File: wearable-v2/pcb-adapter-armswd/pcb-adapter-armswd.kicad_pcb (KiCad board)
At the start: 2 copper layers, 10.6 x 20.8 mm, 2 parts, among them J1 Arm SWD Socket, J2 HERALD_V2_CONN_RECEPTACLE_ARM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

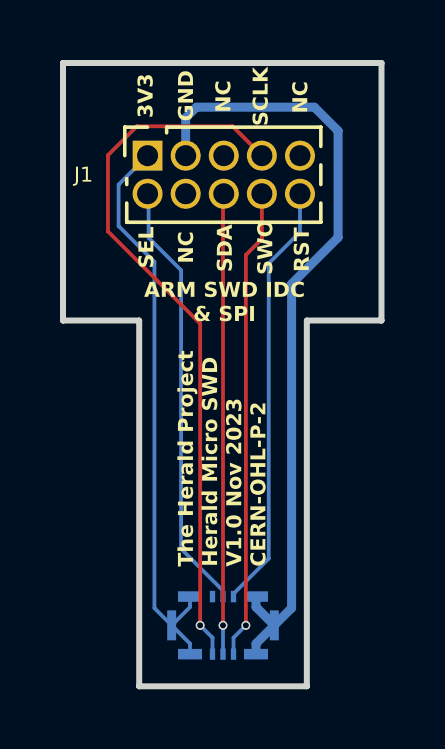
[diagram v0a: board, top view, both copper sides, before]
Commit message: Reworked boards for JLCPCB manufacture
Slightly larger Vias.
Added debug pin holes for Beta testing.
Signed-off-by: Adam Fowler <adam@adamfowler.org>
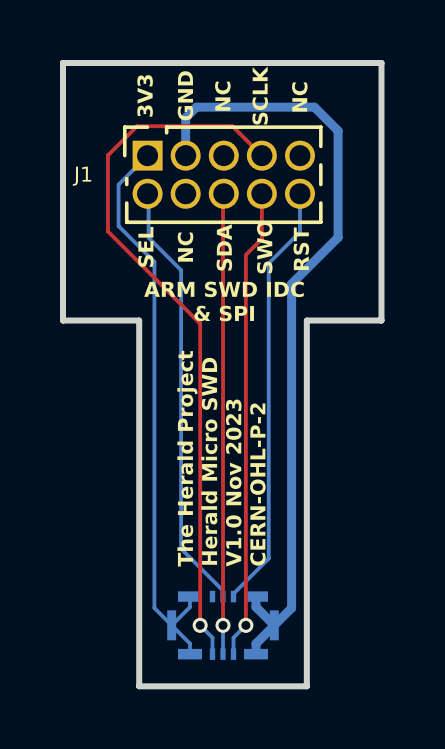
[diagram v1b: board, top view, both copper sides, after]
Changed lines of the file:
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@@
     (grid_origin 139.0396 93.726)
     (pcbplotparams
-      (layerselection 0x00010fc_ffffffff)
+      (layerselection 0x00310fc_ffffffff)
       (plot_on_all_layers_selection 0x0000000_00000000)
       (disableapertmacros false)
@@
       (svgprecision 4)
       (plotframeref false)
-      (viasonmask false)
+      (viasonmask true)
       (mode 1)
       (useauxorigin true)
@@
   (segment (start 135.2042 78.0542) (end 136.1694 77.089) (width 0.127) (layer "F.Cu") (net 3))
   (segment (start 136.1694 77.089) (end 139.3544 77.089) (width 0.127) (layer "F.Cu") (net 3))
-  (via (at 138.2776 93.726) (size 0.3) (drill 0.2) (layers "F.Cu" "B.Cu") (net 3))
+  (via (at 138.2776 93.726) (size 0.5) (drill 0.3) (layers "F.Cu" "B.Cu") (net 3))
   (segment (start 138.6896 94.686) (end 138.6896 94.138) (width 0.127) (layer "B.Cu") (net 3))
   (segment (start 138.6896 94.138) (end 138.2776 93.726) (width 0.127) (layer "B.Cu") (net 3))
@@
   (segment (start 139.0396 93.726) (end 139.0396 79.365) (width 0.127) (layer "F.Cu") (net 5))
   (segment (start 139.0396 79.365) (end 139.065 79.3396) (width 0.127) (layer "F.Cu") (net 5))
-  (via (at 139.0396 93.726) (size 0.3) (drill 0.2) (layers "F.Cu" "B.Cu") (net 5))
+  (via (at 139.0396 93.726) (size 0.5) (drill 0.3) (layers "F.Cu" "B.Cu") (net 5))
   (segment (start 139.0396 93.726) (end 139.0396 94.686) (width 0.127) (layer "B.Cu") (net 5))
   (segment (start 140.5636 91.50042) (end 140.5636 81.661) (width 0.127) (layer "B.Cu") (net 6))
@@
   (segment (start 140.335 80.8482) (end 139.8016 81.3816) (width 0.127) (layer "F.Cu") (net 10))
   (segment (start 139.8016 81.3816) (end 139.8016 93.726) (width 0.127) (layer "F.Cu") (net 10))
-  (via (at 139.8016 93.726) (size 0.3) (drill 0.2) (layers "F.Cu" "B.Cu") (net 10))
+  (via (at 139.8016 93.726) (size 0.5) (drill 0.3) (layers "F.Cu" "B.Cu") (net 10))
   (segment (start 139.3896 94.686) (end 139.3896 94.138) (width 0.127) (layer "B.Cu") (net 10))
   (segment (start 139.3896 94.138) (end 139.8016 93.726) (width 0.127) (layer "B.Cu") (net 10))
